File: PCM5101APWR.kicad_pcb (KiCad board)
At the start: 2 copper layers, 81 x 48.4 mm, 28 parts, among them J1 AudioJack2, J2 AudioJack2, J4 AudioJack2, U1 PCM5101A

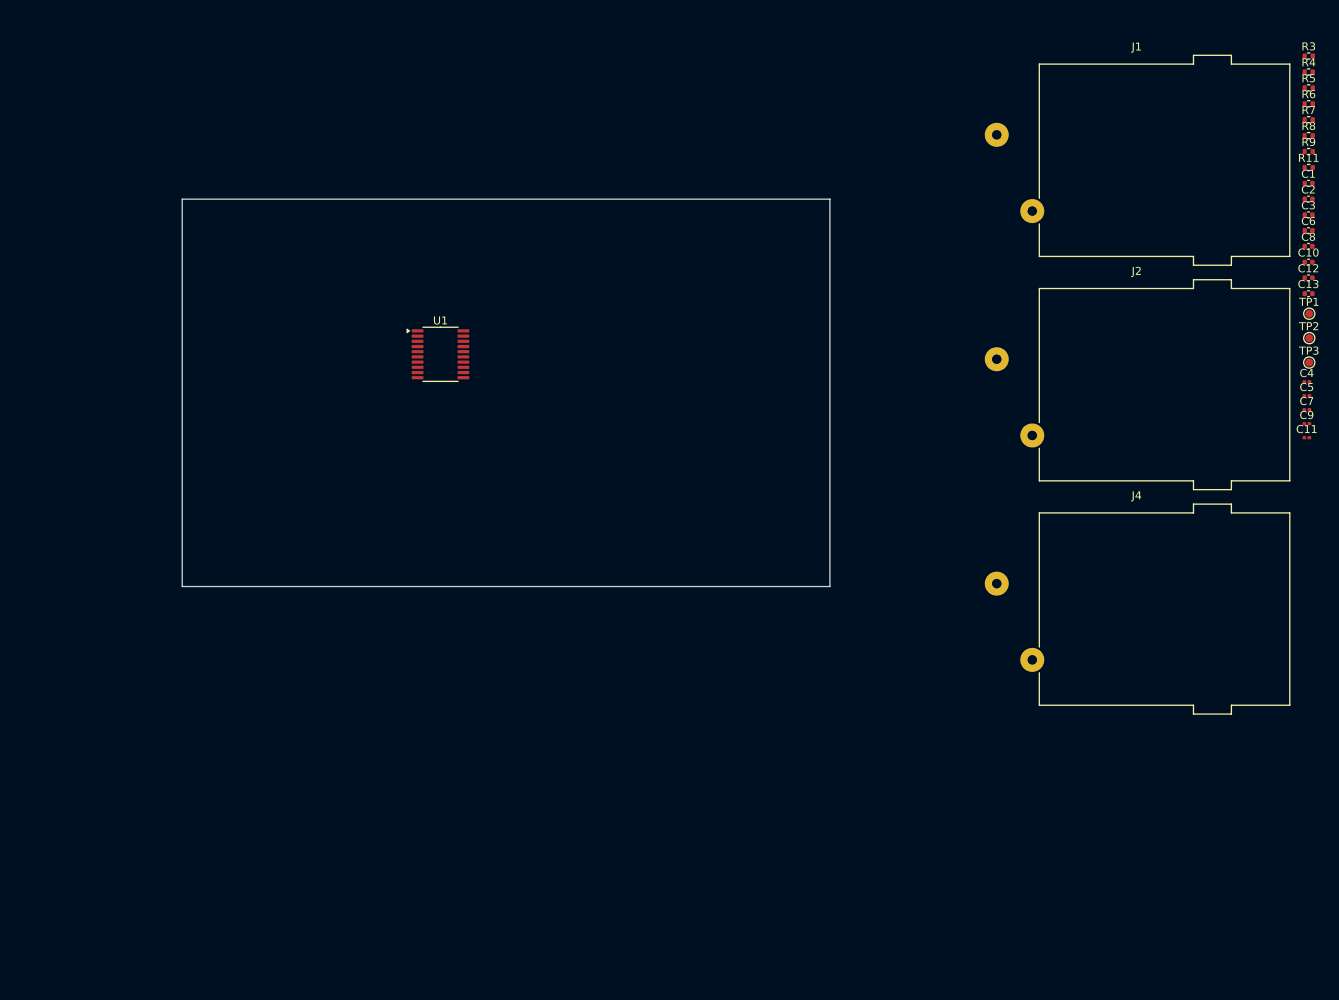
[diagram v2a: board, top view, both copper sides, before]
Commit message: sch done. PCB started
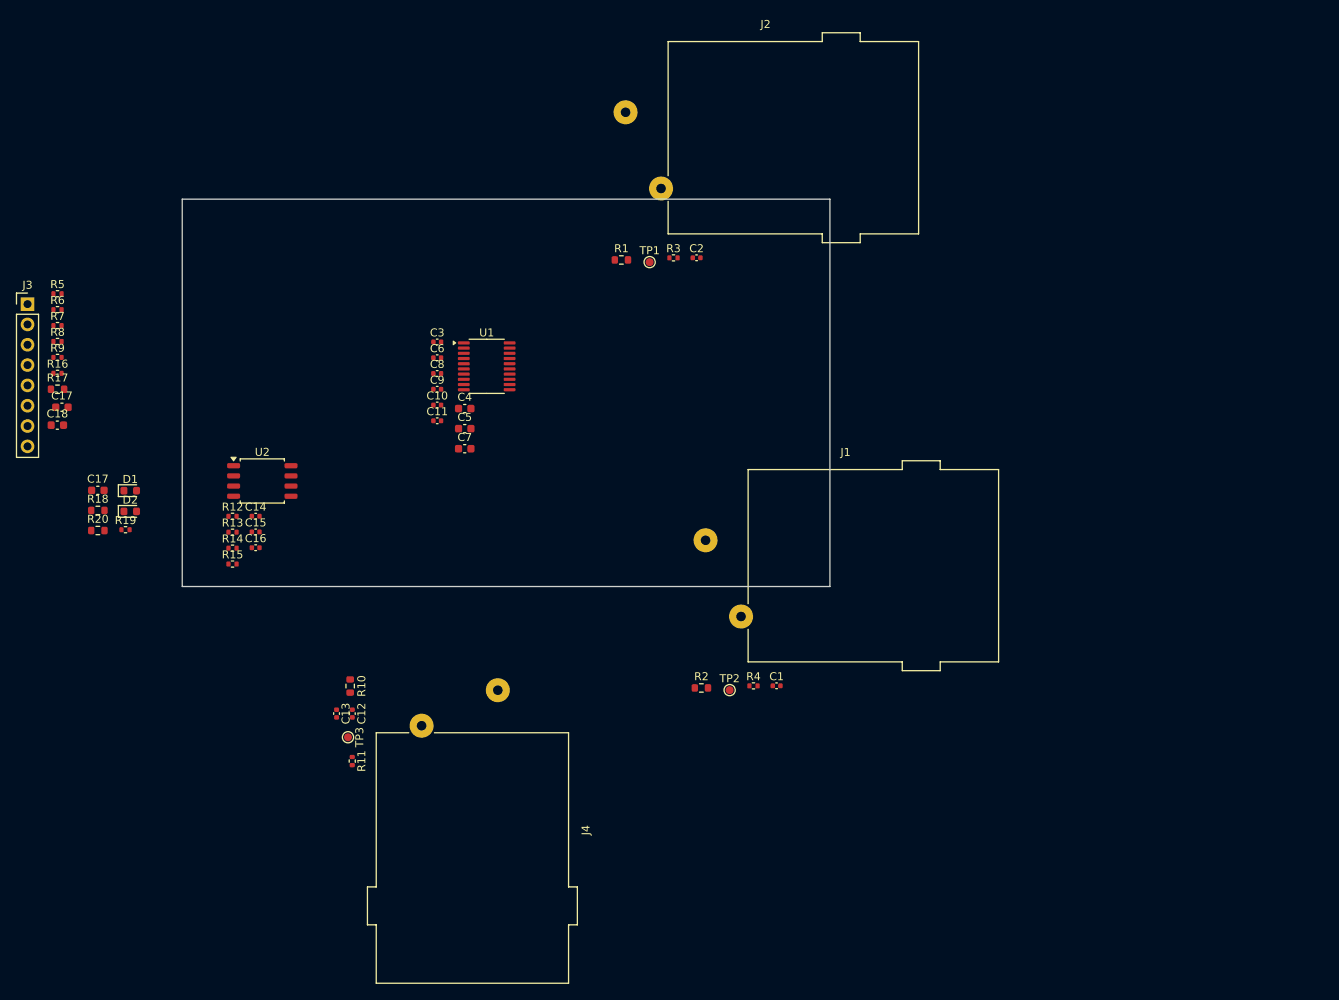
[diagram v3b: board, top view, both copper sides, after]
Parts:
- added C14: 100n, Capacitor_SMD:C_0402_1005Metric, F.Cu at (109.3, 107.3)
- added C15: 2.2u, Capacitor_SMD:C_0402_1005Metric, F.Cu at (109.3, 109.3)
- added C16: 100n, Capacitor_SMD:C_0402_1005Metric, F.Cu at (109.3, 111.2)
- added C17: 10u, Capacitor_SMD:C_0603_1608Metric, F.Cu at (85.0, 93.7)
- added C17: 100n, Capacitor_SMD:C_0603_1608Metric, F.Cu at (89.5, 104.1)
- added C18: 100n, Capacitor_SMD:C_0603_1608Metric, F.Cu at (84.5, 95.9)
- added D1: LED, LED_SMD:LED_0603_1608Metric, F.Cu at (93.6, 104.1)
- added D2: LED, LED_SMD:LED_0603_1608Metric, F.Cu at (93.6, 106.7)
- added J3: Conn_01x08, Connector_PinHeader_2.54mm:PinHeader_1x08_P2.54mm_Vertical, F.Cu at (80.7, 80.8)
- added R1: 470, Resistor_SMD:R_0603_1608Metric, F.Cu at (155.0, 75.3)
- added R10: 470, Resistor_SMD:R_0603_1608Metric, F.Cu at (121.1, 128.5)
- added R12: 100k, Resistor_SMD:R_0402_1005Metric, F.Cu at (106.4, 107.3)
- added R13: 100k, Resistor_SMD:R_0402_1005Metric, F.Cu at (106.4, 109.3)
- added R14: 100k, Resistor_SMD:R_0402_1005Metric, F.Cu at (106.4, 111.3)
- added R15: 100k, Resistor_SMD:R_0402_1005Metric, F.Cu at (106.4, 113.3)
- added R16: 1k, Resistor_SMD:R_0402_1005Metric, F.Cu at (84.5, 89.5)
- added R17: 100, Resistor_SMD:R_0603_1608Metric, F.Cu at (84.5, 91.4)
- added R18: 470, Resistor_SMD:R_0603_1608Metric, F.Cu at (89.5, 106.6)
- added R19: 1k, Resistor_SMD:R_0402_1005Metric, F.Cu at (93.0, 109.0)
- added R2: 470, Resistor_SMD:R_0603_1608Metric, F.Cu at (165.0, 128.8)
- added R20: 0, Resistor_SMD:R_0603_1608Metric, F.Cu at (89.5, 109.1)
- added U2: MCP6002-xSN, Package_SO:SOIC-8_5.3x5.3mm_P1.27mm, F.Cu at (110.1, 102.9)
- C11, C9: footprint Capacitor_SMD:C_0201_0603Metric -> Capacitor_SMD:C_0402_1005Metric
- C4, C5, C7: footprint Capacitor_SMD:C_0201_0603Metric -> Capacitor_SMD:C_0603_1608Metric
- moved R5 158.5 mm to (84.5, 79.5)
- moved R6 158.5 mm to (84.5, 81.5)
- moved R7 158.5 mm to (84.5, 83.5)
- moved R8 158.5 mm to (84.5, 85.5)
- moved R9 158.5 mm to (84.5, 87.5)
- moved R11 140.7 mm to (121.3, 137.9), turned to -90 degrees
- moved C13 132.3 mm to (119.4, 132.0), turned to -90 degrees
- moved C12 131.3 mm to (121.3, 132.0), turned to -90 degrees
- moved TP3 129.0 mm to (120.8, 134.9), turned to -90 degrees
- moved C10 110.4 mm to (132.0, 93.4)
- moved C3 110.1 mm to (132.0, 85.5)
- moved C6 110.1 mm to (132.0, 87.5)
- moved C8 110.1 mm to (132.0, 89.5)
- moved C9 108.8 mm to (132.0, 91.4)
- moved C11 108.7 mm to (132.0, 95.4)
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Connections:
- net Net-(U1-LRCK) renamed /LRCK_IC
- R5 pad 1: Net-(J3-Pin_3) -> /LRCK_CONN
